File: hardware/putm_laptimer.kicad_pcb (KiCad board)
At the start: 4 copper layers, 90 x 63.5 mm, 47 parts, among them J1 Conn_01x22, J10 Conn_01x07, J11 Conn_01x07, J2 Conn_01x22, J3 Conn_01x22, J4 Conn_01x22, J5 2091-1372, J6 2091-1372, J7 Conn_02x05_Odd_Even, J8 Conn_01x09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

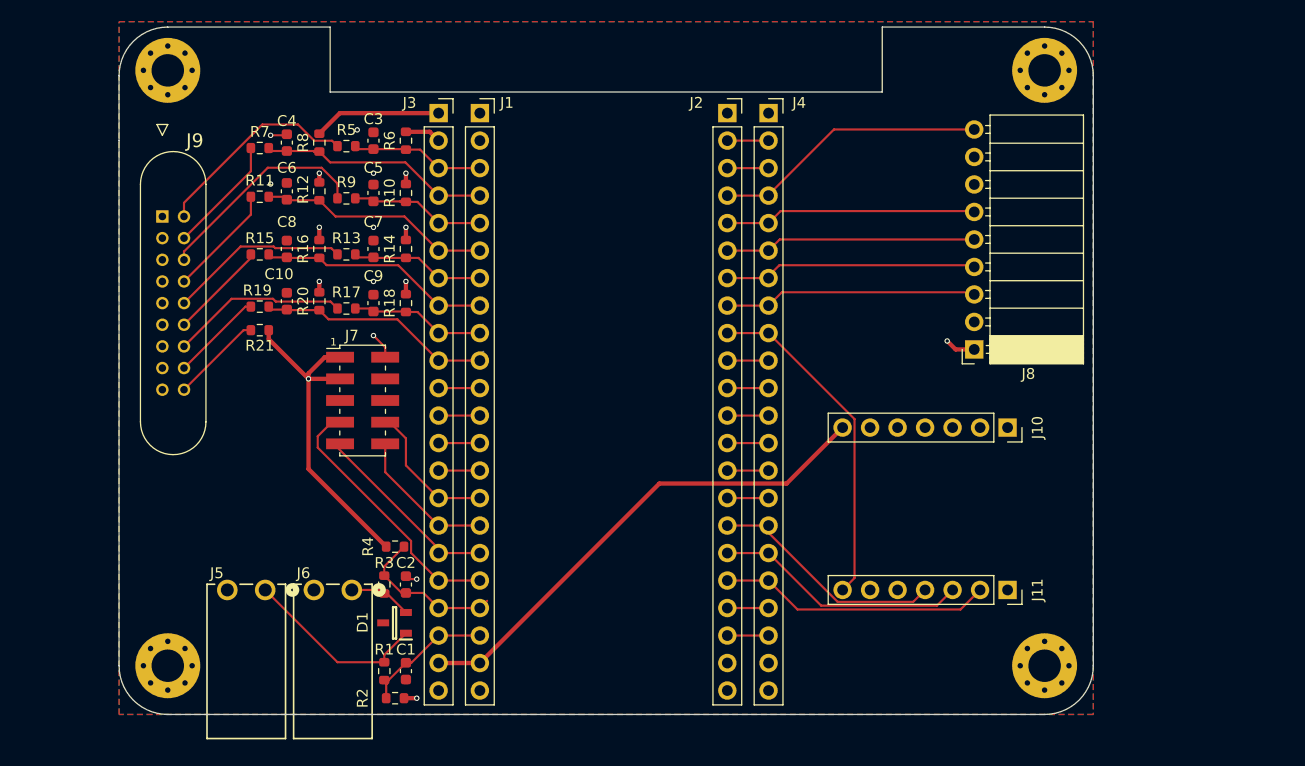
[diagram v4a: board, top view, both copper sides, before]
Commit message: Added connectors for step-up converter and changed wago connectors to 6-pin
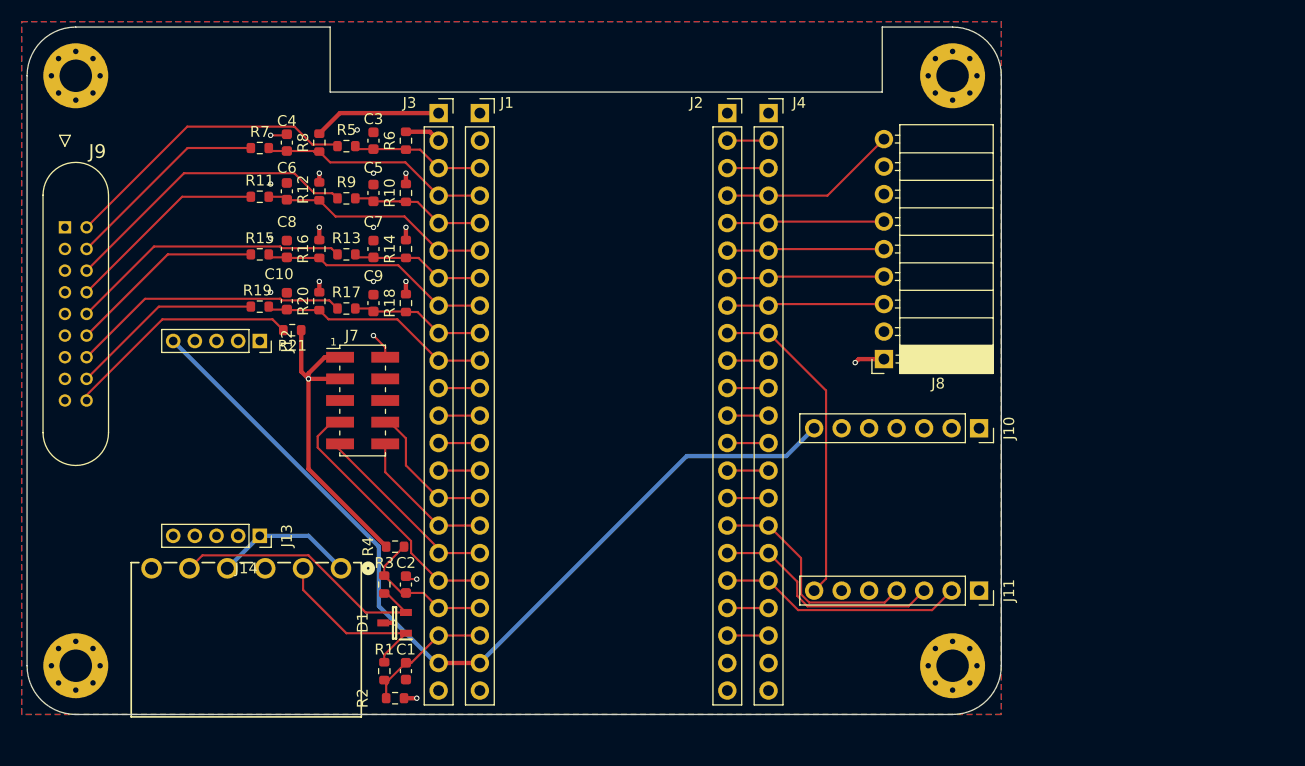
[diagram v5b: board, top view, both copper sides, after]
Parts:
- removed J5, J6: 2091-1372, Footprint:CONN2_2091-1372_WAG
- added J12: Conn_01x05, Connector_PinSocket_2.00mm:PinSocket_1x05_P2.00mm_Vertical, F.Cu at (129.0, 81.5)
- added J13: Conn_01x05, Connector_PinSocket_2.00mm:PinSocket_1x05_P2.00mm_Vertical, F.Cu at (129.0, 99.5)
- added J14: 2091-1376, Footprint:CONN6_2091-1376_WAG, F.Cu at (136.5, 102.5)
- moved J9 9.06 mm to (111.0, 71.0)
- moved REF** 8.51 mm to (112.0, 57.0)
- moved REF** 8.51 mm to (193.0, 57.0)
- moved REF** 8.50 mm to (193.0, 111.5)
- moved REF** 8.50 mm to (112.0, 111.5)
- moved J8 8.39 mm to (186.7, 83.2)
- moved R21 3.00 mm to (132.0, 80.5)
- moved J10 2.63 mm to (195.4, 89.6)
- moved J11 2.63 mm to (195.4, 104.6)
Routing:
- net +5V: track 46.3 -> 83.7 mm
- net Net-(D1-Pad2): track 6.11 -> 25.9 mm
- net /PWR_LED: track 8.45 -> 22.0 mm
- net +12V: track 0.00 -> 13.0 mm
- net /ADD2_BTN: track 8.53 -> 17.9 mm
- net /OC_BTN: track 16.6 -> 26.1 mm
- net /ADD1_BTN: track 16.4 -> 25.8 mm
- net /DRIVER_BTN: track 9.06 -> 18.3 mm
- net /IO41_SD_SPI_MOSI: track 23.5 -> 14.5 mm
- net /IO40_SD_SPI_MISO: track 23.4 -> 14.5 mm
- net /IO2_SD_SPI_CS: track 23.3 -> 14.5 mm
- net /IO1_SD_CD: track 25.4 -> 16.6 mm
- net /IO42_SD_SPI_CLK: track 23.2 -> 14.5 mm
- net /RST_BTN: track 19.3 -> 27.8 mm
- net /DOO_BTN: track 10.4 -> 18.8 mm
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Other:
- outline, holes or cut-outs redrawn

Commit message: Changed layout
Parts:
- moved REF** 11.0 mm to (204.0, 111.0)
- moved REF** 11.0 mm to (204.0, 57.0)
- moved J8 10.9 mm to (197.6, 83.2)
- moved J10 9.64 mm to (205.1, 90.0)
- moved J11 9.64 mm to (205.1, 104.9)
- moved C1 9.00 mm to (151.5, 112.0)
- moved C10 9.00 mm to (140.5, 77.8)
- moved C2 9.00 mm to (151.5, 104.0)
- moved C3 9.00 mm to (148.5, 63.0)
- moved C4 9.00 mm to (140.5, 63.2)
- moved C5 9.00 mm to (148.5, 67.8)
- moved C6 9.00 mm to (140.5, 67.7)
- moved C7 9.00 mm to (148.5, 73.0)
- moved C8 9.00 mm to (140.5, 73.0)
- moved C9 9.00 mm to (148.5, 78.0)
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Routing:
- net /IO42_SD_SPI_CLK: track 14.5 -> 16.5 mm
- net /IO41_SD_SPI_MOSI: track 14.5 -> 16.5 mm
- net /IO40_SD_SPI_MISO: track 14.5 -> 16.5 mm
- net /IO2_SD_SPI_CS: track 14.5 -> 16.5 mm
- net /IO1_SD_CD: track 16.6 -> 18.6 mm
- net Net-(D1-Pad2): track 25.9 -> 26.9 mm
- net /IO47_RTC_I2C_SDA: track 21.6 -> 22.4 mm
- net /IO48_RTC_CLKOUT: track 21.0 -> 21.8 mm
- net /IO21_RTC_I2C_SCL: track 22.6 -> 23.4 mm
- net +5V: track 83.7 -> 84.4 mm
- net /IO39_RTC_NINT: track 30.3 -> 30.9 mm
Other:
- board size 90 x 63.5 mm -> 92 x 63.5 mm
- board text added: "5V/12V CONVERTER"
- board text added: "RTC"

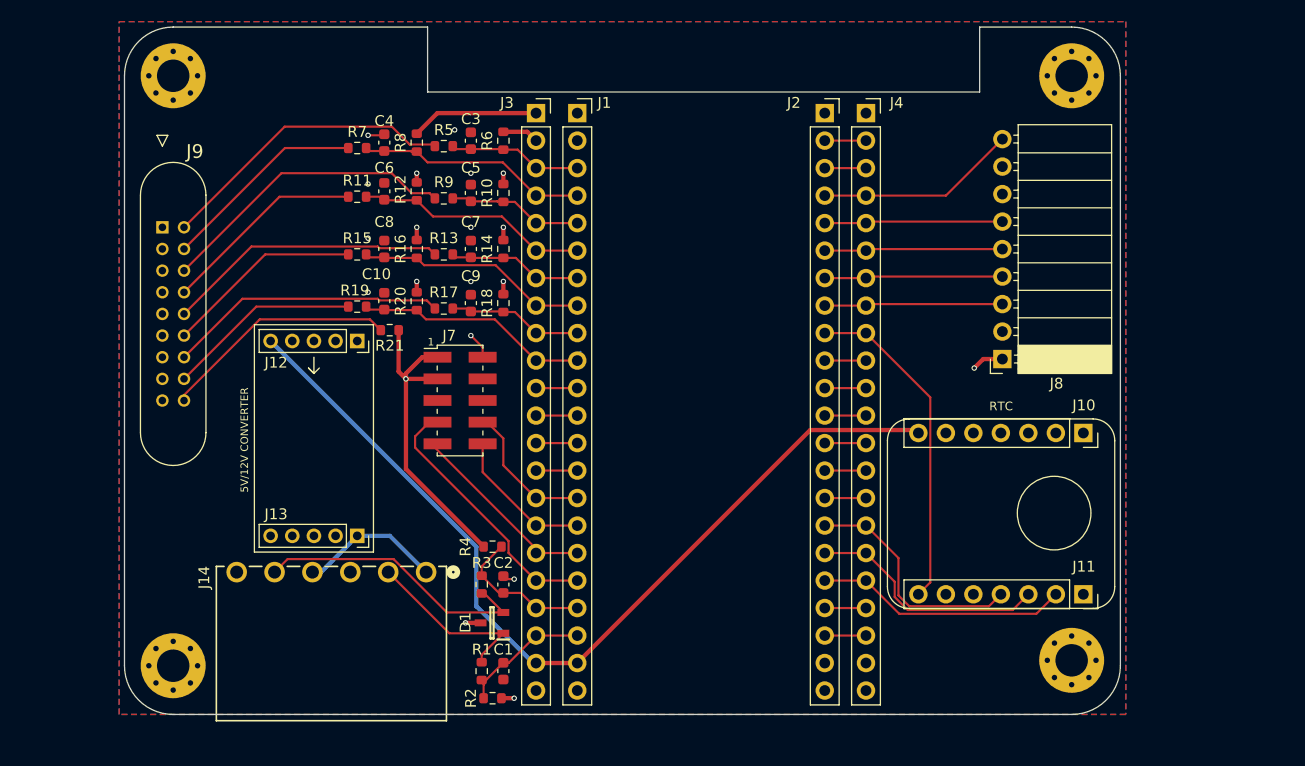
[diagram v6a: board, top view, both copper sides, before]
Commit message: Fixed connector footprint
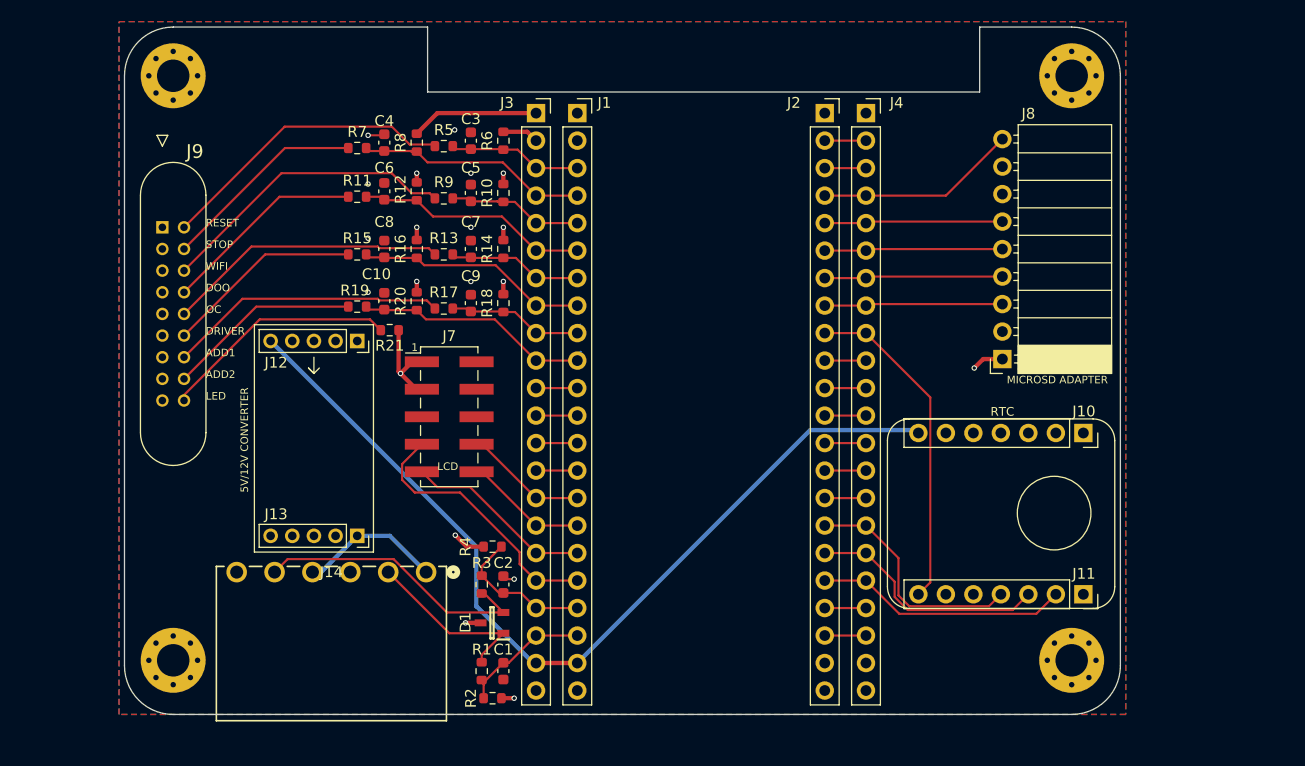
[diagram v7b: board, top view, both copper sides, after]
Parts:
- J7: footprint Connector_PinHeader_2.00mm:PinHeader_2x05_P2.00mm_Vertical_SMD -> Connector_PinHeader_2.54mm:PinHeader_2x05_P2.54mm_Vertical_SMD
- moved J7 1.80 mm to (146.5, 88.5)
- moved REF** 0.50 mm to (121.0, 111.0)
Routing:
- net +3V3: track 56.8 -> 38.7 mm, vias 9 -> 10
- net GND: track 6.50 -> 4.06 mm, vias 11 -> 10
- net /IO10_LCD_SPI_CS: track 13.4 -> 11.4 mm
- net /IO9_LCD_SPI_MOSI: track 12.7 -> 11.4 mm
- net /IO12_LCD_DC: track 23.8 -> 24.7 mm
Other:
- board text added: "ADD1"
- board text added: "ADD2"
- board text added: "DOO"
- board text added: "DRIVER"
- board text added: "LCD"
- board text added: "LED"
- board text added: "OC"
- board text added: "RESET"
- board text added: "STOP"
- board text added: "WIFI"
